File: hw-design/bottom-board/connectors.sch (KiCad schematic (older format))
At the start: 24 parts, among them J1 JACK_TRS_6PINS, J2 JACK_TRS_6PINS, J3 JACK_TRS_6PINS, J4 JACK_TRS_6PINS, J5 JACK_TRS_6PINS, J6 RJ45_LEDS, P5 BARREL_JACK, P7 CONN_01X10, P8 CONN_02X10, P9 CONN_01X03

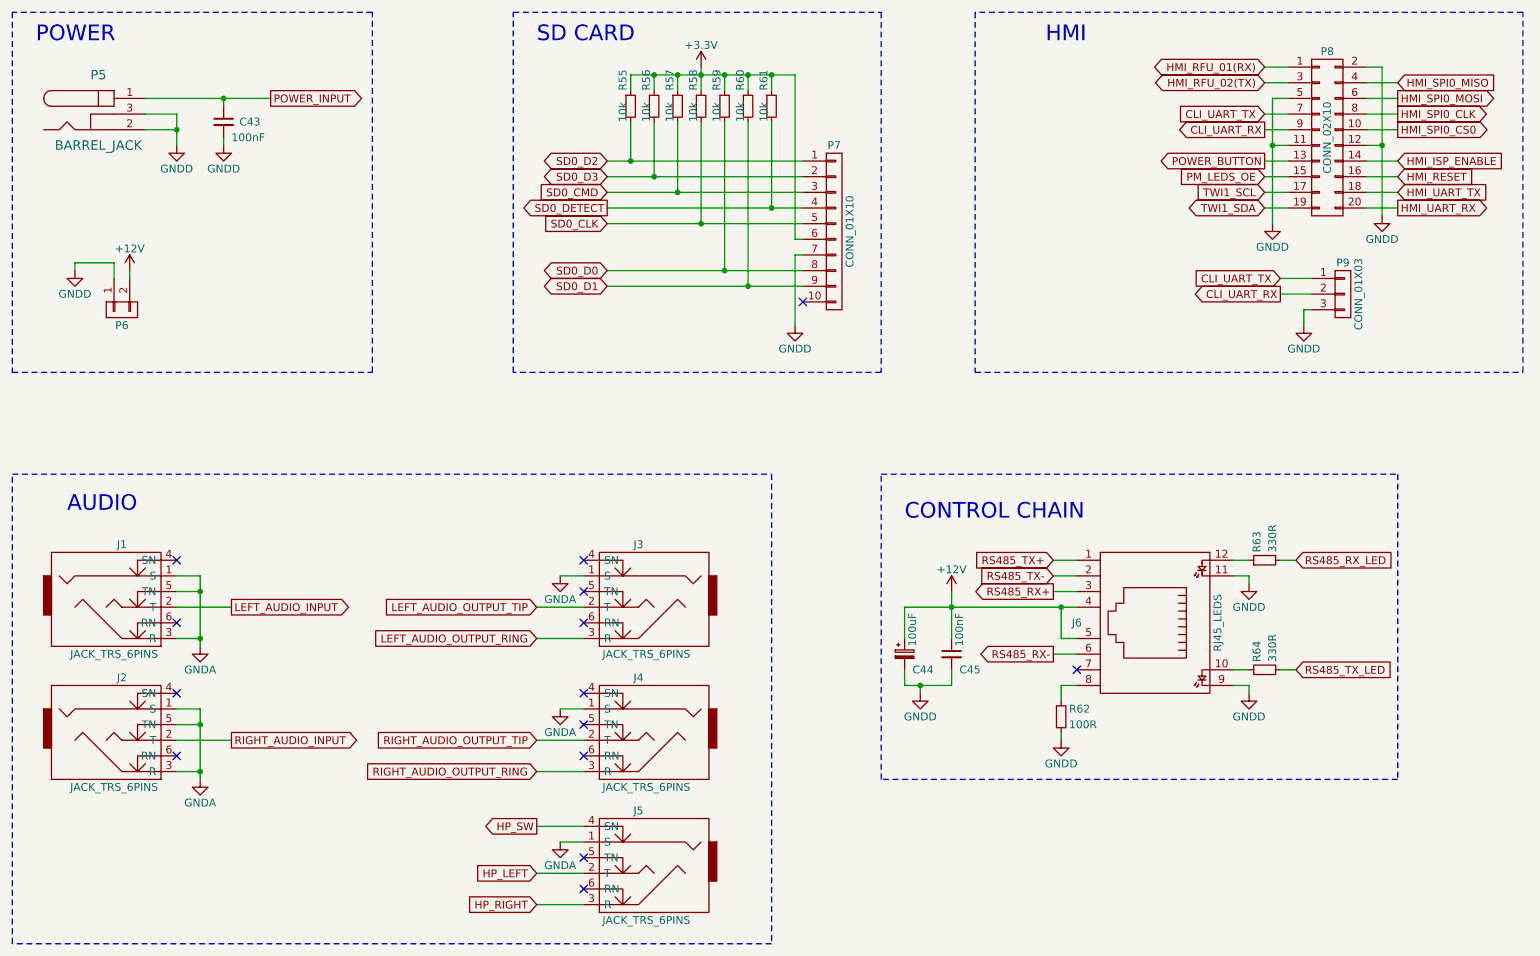
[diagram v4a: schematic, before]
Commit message: sch,bottom-board: new HMI power connector
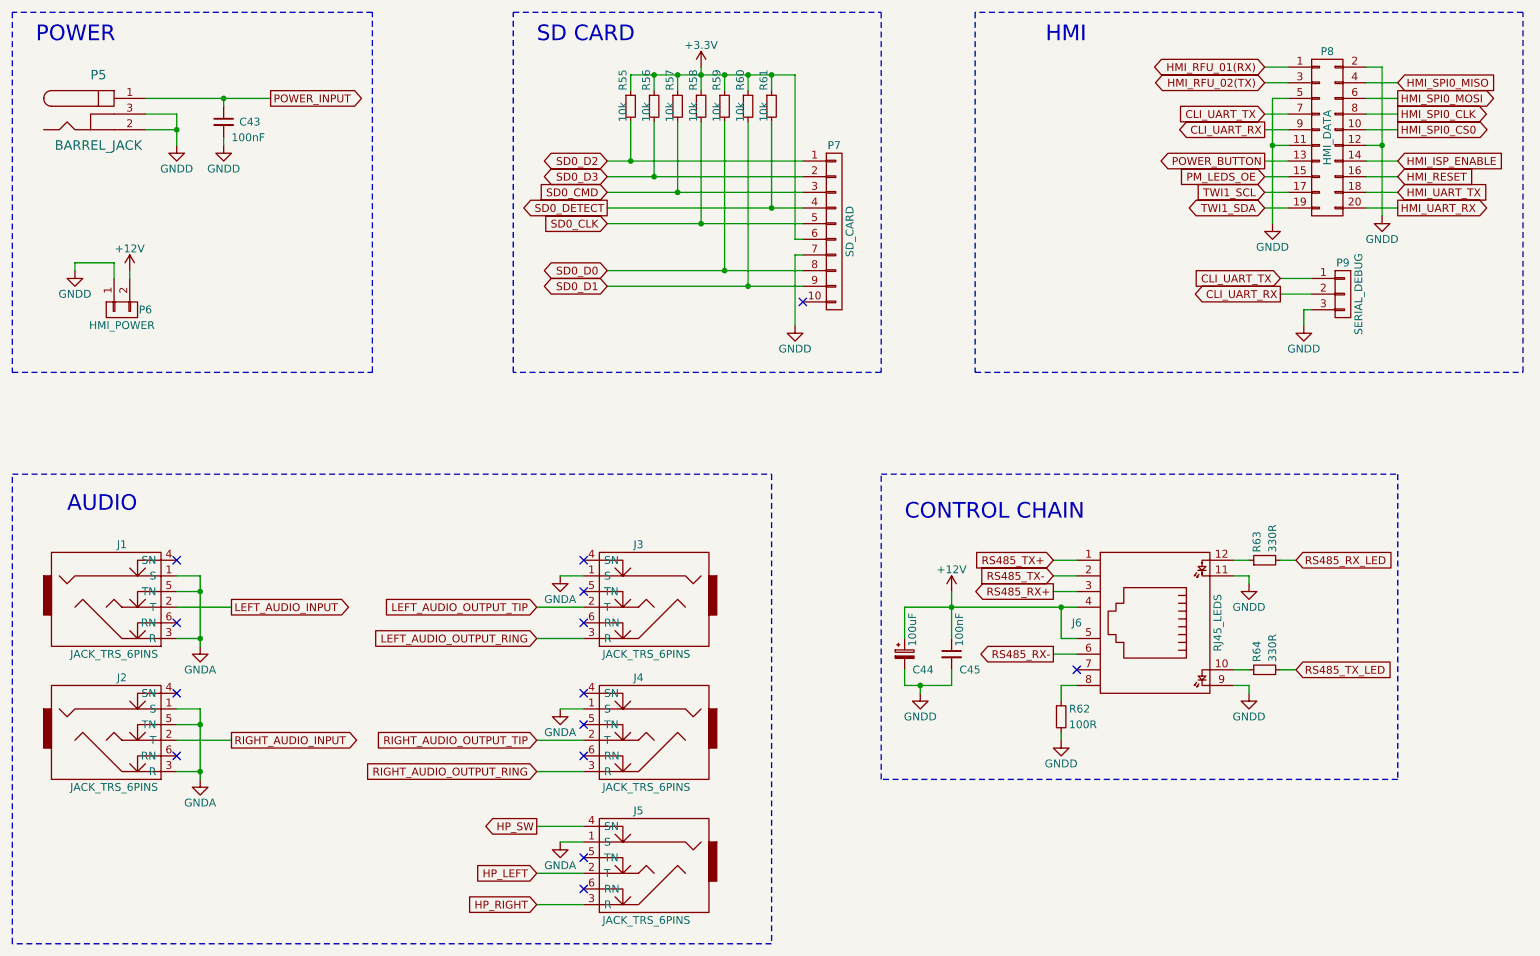
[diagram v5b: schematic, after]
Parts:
- P6: value ~ -> HMI_POWER; footprint footprints:Pin_Header_Straight_1x02_Pitch2.00mm_Shrouded -> footprints:B2B-XH-A; MPN 440054-2 -> B2B-XH-A(LF)(SN)
- P7: value CONN_01X10 -> SD_CARD
- P8: value CONN_02X10 -> HMI_DATA
- P9: value CONN_01X03 -> SERIAL_DEBUG
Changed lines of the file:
@@
 P 9650 1650
 F 0 "P8" H 9650 2200 50  0000 C CNN
-F 1 "CONN_02X10" V 9650 1650 50  0000 C CNN
+F 1 "HMI_DATA" V 9650 1650 50  0000 C CNN
 F 2 "footprints:Pin_Header_Straight_2x10_Shrouded" H 9650 450 60  0001 C CNN
 F 3 "" H 9650 450 60  0000 C CNN
@@
 U 1 1 550C4D2F
 P 1950 2750
-F 0 "P6" V 2050 2750 50  0000 C CNN
-F 1 "~" V 2050 2750 50  0000 C CNN
-F 2 "footprints:Pin_Header_Straight_1x02_Pitch2.00mm_Shrouded" H 1950 2750 60  0001 C CNN
+F 0 "P6" V 1950 2600 50  0000 C CNN
+F 1 "HMI_POWER" V 2050 2750 50  0000 C CNN
+F 2 "footprints:B2B-XH-A" H 1950 2750 60  0001 C CNN
 F 3 "" H 1950 2750 60  0000 C CNN
-F 4 "440054-2" H 200 400 50  0001 C CNN "MPN"
+F 4 "B2B-XH-A(LF)(SN)" H 200 400 50  0001 C CNN "MPN"
 	1    1950 2750
 	0    -1   1    0
@@
 P 9750 2650
 F 0 "P9" H 9750 2850 50  0000 C CNN
-F 1 "CONN_01X03" V 9850 2650 50  0000 C CNN
+F 1 "SERIAL_DEBUG" V 9850 2650 50  0000 C CNN
 F 2 "Pin_Headers:Pin_Header_Straight_1x03" H 9750 2650 60  0001 C CNN
 F 3 "" H 9750 2650 60  0000 C CNN
@@
 P 6500 2250
 F 0 "P7" H 6500 2800 50  0000 C CNN
-F 1 "CONN_01X10" V 6600 2250 50  0000 C CNN
+F 1 "SD_CARD" V 6600 2250 50  0000 C CNN
 F 2 "Pin_Headers:Pin_Header_Straight_1x10" H 6500 2250 60  0001 C CNN
 F 3 "" H 6500 2250 60  0000 C CNN

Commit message: sch,bottom-board: fix jack connectors PN
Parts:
- J1, J2, J3, J4, J5: MPN NMJ6HCD2-RM -> NMJ6HCD2
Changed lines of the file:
@@
 F 2 "Connect:NMJ6HCD2" H 2050 5350 60  0001 C CNN
 F 3 "" H 2050 5350 60  0000 C CNN
-F 4 "NMJ6HCD2-RM" H 0   -200 50  0001 C CNN "MPN"
+F 4 "NMJ6HCD2" H 0   -200 50  0001 C CNN "MPN"
 	1    1900 5500
 	1    0    0    -1
@@
 F 2 "Connect:NMJ6HCD2" H 2050 4500 60  0001 C CNN
 F 3 "" H 2050 4500 60  0000 C CNN
-F 4 "NMJ6HCD2-RM" H 0   -200 50  0001 C CNN "MPN"
+F 4 "NMJ6HCD2" H 0   -200 50  0001 C CNN "MPN"
 	1    1900 4650
 	1    0    0    -1
@@
 F 2 "Connect:NMJ6HCD2" H 5450 4500 60  0001 C CNN
 F 3 "" H 5450 4500 60  0000 C CNN
-F 4 "NMJ6HCD2-RM" H 0   -200 50  0001 C CNN "MPN"
+F 4 "NMJ6HCD2" H 0   -200 50  0001 C CNN "MPN"
 	1    5300 4650
 	-1   0    0    -1
@@
 F 2 "Connect:NMJ6HCD2" H 5450 5350 60  0001 C CNN
 F 3 "" H 5450 5350 60  0000 C CNN
-F 4 "NMJ6HCD2-RM" H 0   -200 50  0001 C CNN "MPN"
+F 4 "NMJ6HCD2" H 0   -200 50  0001 C CNN "MPN"
 	1    5300 5500
 	-1   0    0    -1
@@
 F 2 "Connect:NMJ6HCD2" H 5450 6200 60  0001 C CNN
 F 3 "" H 5450 6200 60  0000 C CNN
-F 4 "NMJ6HCD2-RM" H 0   -200 50  0001 C CNN "MPN"
+F 4 "NMJ6HCD2" H 0   -200 50  0001 C CNN "MPN"
 	1    5300 6350
 	-1   0    0    -1
